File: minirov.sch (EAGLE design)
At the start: 69 parts, among them Q1 DMN6140L-13DICT-ND, Q2 DMN6140L-13DICT-ND, U1 DRV8848PWP, U2 DRV8848PWP, Y1 ECS-80-S-4X

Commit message: first iteration of schematic and board placements
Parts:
- removed C1, C10, C2, C3, C4, C5, C6, C7, C8, C9: 4.7uF, SparkFun-Capacitors:4.7UF0603
- removed C11: 0.1uF, SparkFun-Capacitors:0.1UF-0603-25V-(+80/-20%)
- removed R1, R10, R11, R2, R3: 1k, SparkFun-Resistors:1KOHM-0603-1/10W-1%
- removed RESET: SWITCH, DiscreteComponents:SWITCH
- removed SV1: (no value), con-lsta:FE05-1
- removed Y1: ECS-80-S-4X, ECS-80-S-4X:ECS-80-S-4X
- added C19: 100nF, SparkFun-Capacitors:10NF-0603-50V-10%
- added J21: (no value), SparkFun-Connectors:CONN_01
- added U$8: TLE493DW2B6, TLE493DW2B6:TLE493DW2B6
- added U$9: RPI-ZERO, RPI-Zero:RPI-ZERO
- U$2: value TCAN337D -> 74CBTLV3257PW; device PI_Shield_Library:TCAN337D -> 74CBTLV3257PW:74CBTLV3257PW
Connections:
- removed net N$3: C11.2, R10.1, R11.2
- removed net NRST: C7.1, R2.1, RESET.P$2, SV1.2, U$1.NRST
- removed net PWM3: U2.AIN1
- removed net PWM4: U2.AIN2
- new net MTR1_PWM: U$2.1A, U$9.GPIO13
- new net MTR2_PWM: U$2.2A, U$9.GPIO18
- new net MTR_AB_SEL: U$2.S, U$9.GEN4/GPIO23
- new net MTR_NOE: U$2.NOE, U$9.GPIO22/GEN3
- net +3V3: now also C19.2, J21.1, U$2.3V3, U$8.3V3; no longer C1.1, C10.1, C2.1, C3.1, C4.1, C5.1, C6.1, R2.2, SV1.5, U$1.VDD, U$1.VDDA, U$1.VDDIO2, U$2.VCC
- net +5V: now also U$9.5V0@1, U$9.5V0@2
- net CAN_H: no longer R10.2, U$2.CANH
- net CAN_L: no longer R11.1, U$2.CANL
- net CAN_STM_RX: no longer U$2.TXD
- net CAN_STM_TX: no longer U$2.RXD
- net GND: now also C19.1, U$8.GND1, U$8.GND2, U$8.GND3, U$9.GND@1, U$9.GND@2, U$9.GND@3, U$9.GND@4, U$9.GND@5, U$9.GND@6, U$9.GND@7, U$9.GND@8; no longer C1.2, C10.2, C11.1, C2.2, C3.2, C4.2, C5.2, C6.2, C7.2, C8.2, C9.2, RESET.P$1, SV1.1
- net LED1_PWM: now also U$9.GPIO17/GEN0; no longer U$1.PA6
- net LED2_PWM: now also U$9.GPIO27/GEN2; no longer U$1.PA7
- net MISO: now also U$9.GPIO9/MISO; no longer U$1.PB4
- net MOSI: now also U$9.GPIO10/MOSI; no longer U$1.PB5
- net MTR_1A_PWM: now also U$2.1B1; no longer U$1.PA0
- net MTR_1B_PWM: now also U$2.1B2; no longer U$1.PA1
- net MTR_2A_PWM: now also U$2.2B1, U2.AIN1; no longer U$1.PA2
- net MTR_2B_PWM: now also U$2.2B2, U2.AIN2; no longer U$1.PA3
- net N$1: now also U$9.TXD0/GPIO14; no longer C9.1, R1.1, Y1.2
- net N$2: now also U$9.RXD0/GPIO15; no longer C8.1, R3.1, Y1.1
- net OSC_IN: no longer R3.2
- net OSC_OUT: no longer R1.2
- net SCK: now also U$9.GPIO11/SCLK; no longer U$1.PB3
- net SCL: now also U$8.SCL, U$9.GPIO3/SCL1; no longer U$1.PB6
- net SDA: now also U$8.SDA, U$9.GPIO2/SDA1; no longer U$1.PB7
- net SWCLK: no longer SV1.3
- net SWDIO: no longer SV1.4
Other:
- note added: "Magnetometer"
- note removed: "CAN TERMINATION"
- note removed: "CAN TRANSCEIVER"
- note removed: "Pin 1 (VDD)"
- note removed: "Pin 17 (VDDIO2)"
- note removed: "Pin 5 (VDDA)"

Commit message: first round of routing. need to gnd stitch
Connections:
- removed net 12V: U$4.VIN
- net +12V: now also U$4.VIN
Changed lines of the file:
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@@
 <pinref part="SUPPLY5" gate="G$1" pin="12V"/>
+</segment>
+<segment>
+<pinref part="U$4" gate="G$1" pin="VIN"/>
+<wire x1="160.02" y1="279.4" x2="152.4" y2="279.4" width="0.1524" layer="91"/>
+<wire x1="152.4" y1="279.4" x2="152.4" y2="281.94" width="0.1524" layer="91"/>
+<pinref part="SUPPLY2" gate="G$1" pin="12V"/>
+<label x="152.4" y="276.86" size="1.778" layer="95"/>
 </segment>
 </net>
@@
 </segment>
 </net>
-<net name="12V" class="0">
-<segment>
-<pinref part="U$4" gate="G$1" pin="VIN"/>
-<wire x1="160.02" y1="279.4" x2="152.4" y2="279.4" width="0.1524" layer="91"/>
-<wire x1="152.4" y1="279.4" x2="152.4" y2="281.94" width="0.1524" layer="91"/>
-<pinref part="SUPPLY2" gate="G$1" pin="12V"/>
-</segment>
-</net>

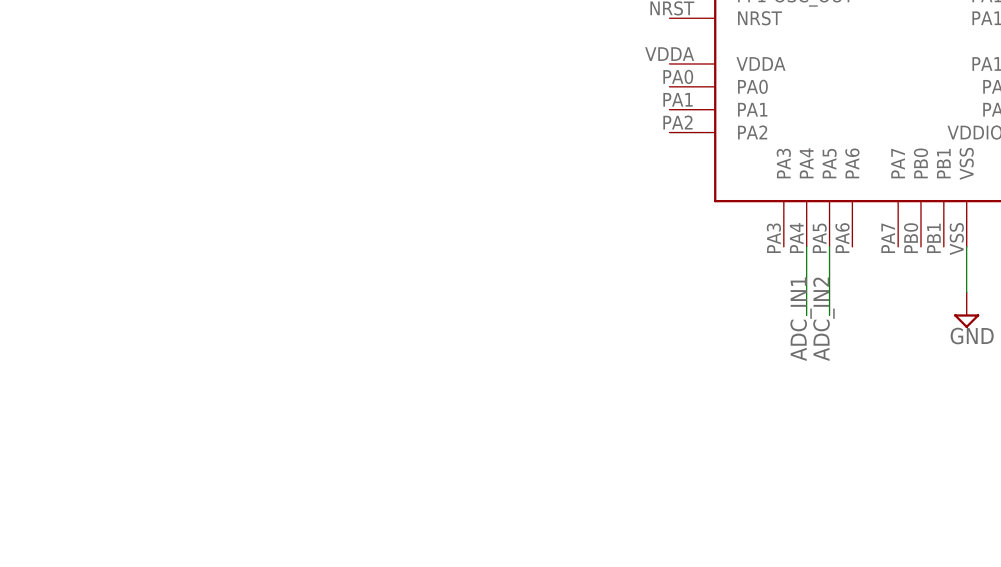
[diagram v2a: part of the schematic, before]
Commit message: added ADC
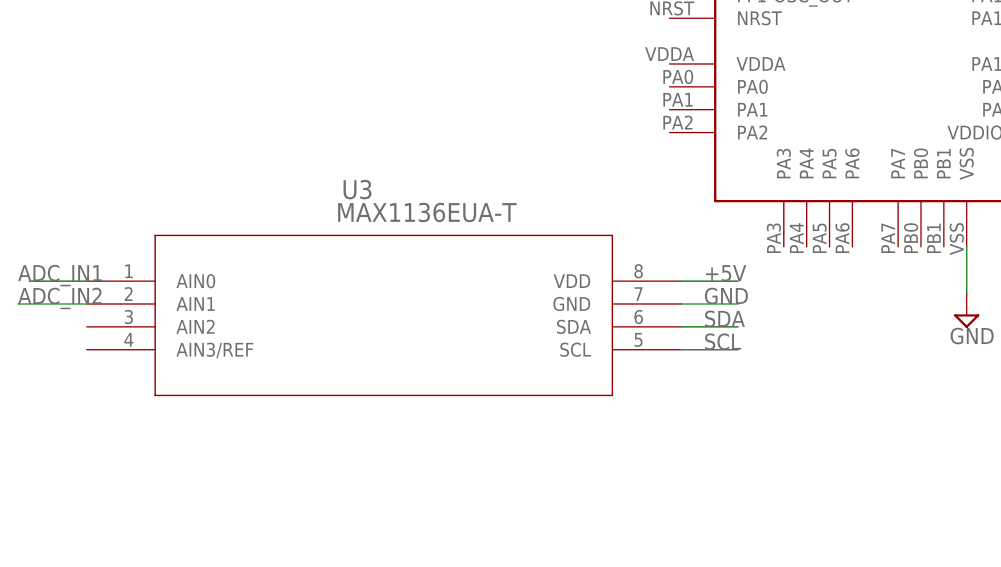
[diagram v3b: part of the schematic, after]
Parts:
- added U3: MAX1136EUA-T, MAX1136EUA-T:MAX1136EUA-T
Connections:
- net +5V: now also U3.VDD
- net ADC_IN1: now also U3.AIN0; no longer U$1.PA4
- net ADC_IN2: now also U3.AIN1; no longer U$1.PA5
- net GND: now also U3.GND
- net SCL: now also U3.SCL
- net SDA: now also U3.SDA
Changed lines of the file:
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@@
 <part name="GND3" library="supply1" library_urn="urn:adsk.eagle:library:371" deviceset="GND" device=""/>
 <part name="J21" library="SparkFun-Connectors" library_urn="urn:adsk.eagle:library:513" deviceset="CONN_01" device="" package3d_urn="urn:adsk.eagle:package:38028/1"/>
+<part name="U3" library="MAX1136EUA-T" deviceset="MAX1136EUA-T" device=""/>
 </parts>
 <sheets>
@@
 </instance>
 <instance part="J21" gate="G$1" x="81.28" y="246.38"/>
+<instance part="U3" gate="A" x="13.97" y="97.79" smashed="yes">
+<attribute name="NAME" x="42.3006" y="106.91988125" size="2.08538125" layer="95" ratio="6" rot="SR0"/>
+<attribute name="VALUE" x="41.6681" y="104.377509375" size="2.08561875" layer="96" ratio="6" rot="SR0"/>
+</instance>
 </instances>
 <busses>
@@
 <pinref part="GND3" gate="1" pin="GND"/>
 </segment>
+<segment>
+<pinref part="U3" gate="A" pin="GND"/>
+<wire x1="80.01" y1="95.25" x2="86.36" y2="95.25" width="0.1524" layer="91"/>
+<label x="82.55" y="95.25" size="1.778" layer="95"/>
+</segment>
 </net>
 <net name="SWDIO" class="0">
@@
 <net name="ADC_IN1" class="0">
 <segment>
-<pinref part="U$1" gate="G$1" pin="PA4"/>
-<wire x1="93.98" y1="101.6" x2="93.98" y2="93.98" width="0.1524" layer="91"/>
-<label x="93.98" y="88.9" size="1.778" layer="95" rot="R90"/>
-</segment>
-<segment>
 <pinref part="J13" gate="G$1" pin="1"/>
 <wire x1="88.9" y1="215.9" x2="96.52" y2="215.9" width="0.1524" layer="91"/>
 <label x="93.98" y="215.9" size="1.778" layer="95"/>
 </segment>
+<segment>
+<pinref part="U3" gate="A" pin="AIN0"/>
+<wire x1="7.62" y1="97.79" x2="13.97" y2="97.79" width="0.1524" layer="91"/>
+<label x="6.35" y="97.79" size="1.778" layer="95"/>
+</segment>
 </net>
 <net name="ADC_IN2" class="0">
-<segment>
-<pinref part="U$1" gate="G$1" pin="PA5"/>
-<wire x1="96.52" y1="101.6" x2="96.52" y2="93.98" width="0.1524" layer="91"/>
-<label x="96.52" y="88.9" size="1.778" layer="95" rot="R90"/>
-</segment>
 <segment>
 <pinref part="J14" gate="G$1" pin="1"/>
@@
 <label x="93.98" y="205.74" size="1.778" layer="95"/>
 </segment>
+<segment>
+<pinref part="U3" gate="A" pin="AIN1"/>
+<wire x1="13.97" y1="95.25" x2="6.35" y2="95.25" width="0.1524" layer="91"/>
+<label x="6.35" y="95.25" size="1.778" layer="95"/>
+</segment>
 </net>
 <net name="SDA" class="0">
@@
 <label x="149.86" y="104.14" size="1.778" layer="95"/>
 </segment>
+<segment>
+<pinref part="U3" gate="A" pin="SDA"/>
+<wire x1="80.01" y1="92.71" x2="86.36" y2="92.71" width="0.1524" layer="91"/>
+<label x="82.55" y="92.71" size="1.778" layer="95"/>
+</segment>
 </net>
 <net name="SCL" class="0">
@@
 <wire x1="157.48" y1="101.6" x2="152.4" y2="101.6" width="0.1524" layer="91"/>
 <label x="149.86" y="101.6" size="1.778" layer="95"/>
+</segment>
+<segment>
+<pinref part="U3" gate="A" pin="SCL"/>
+<wire x1="80.01" y1="90.17" x2="86.36" y2="90.17" width="0.1524" layer="91"/>
+<label x="82.55" y="90.17" size="1.778" layer="95"/>
 </segment>
 </net>
@@
 <label x="215.9" y="106.68" size="1.778" layer="95"/>
 </segment>
-</net>
+<segment>
+<pinref part="U3" gate="A" pin="VDD"/>
+<wire x1="80.01" y1="97.79" x2="86.36" y2="97.79" width="0.1524" layer="91"/>
+<label x="82.55" y="97.79" size="1.778" layer="95"/>
+</segment>
+</net>

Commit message: schematic changes and board changes to reflect it
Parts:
- removed C18: 10uF, SparkFun-Capacitors:10UF-0603-6.3V-20%
- removed D1: (no value), SparkFun-LED:LED0603
- removed J20, J6: (no value), SparkFun-Connectors:CONN_02
- removed J5: (no value), SparkFun-Connectors:CONN_04
- removed R12, R9: 0, SparkFun-Resistors:RESISTOR0603
- removed R6: (no value), SparkFun-Resistors:RESISTOR0603
- removed R7, R8: 10k, SparkFun-Resistors:RESISTOR0603
- removed U$1: STM32F042K6T6, PI_Shield_Library:STM32F042K6T6
- removed U$5: UN2112, minirov:UN2112
- removed U$6: UN2212, minirov:UN2212
- removed U$7: BAS16, minirov:BAS16
- removed U3: MAX1136EUA-T, MAX1136EUA-T:MAX1136EUA-T
- added C1: 100nF, SparkFun-Capacitors:10NF-0603-50V-10%
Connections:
- removed net CAN_H: J5.3
- removed net CAN_L: J5.2
- removed net CAN_STM_RX: U$1.PA11
- removed net CAN_STM_TX: U$1.PA12
- removed net HBEAT_LED: R6.1, U$1.PA15
- removed net N$1: U$9.TXD0/GPIO14
- removed net N$2: U$9.RXD0/GPIO15
- removed net N$4: D1.A, R6.2
- removed net N$5: C18.1, R8.1, U$7.1
- removed net OSC_IN: U$1.PF0-OSC_IN
- removed net OSC_OUT: U$1.PF1-OSC_OUT
- removed net RS-IN: J20.2, U$6.B, U$7.3
- removed net RS-OUT: J20.1, R8.2, U$5.C
- removed net RX: R12.1, U$5.B
- removed net SWCLK: U$1.PA14
- removed net SWDIO: U$1.PA13
- removed net TX: R7.1, R9.1, U$6.C
- removed net USART_RX: J6.1, R12.2, U$1.PA10
- removed net USART_TX: J6.2, R9.2, U$1.PA9
- net +12V: no longer J5.4
- net +3V3: now also C1.1; no longer R7.2, U$5.E
- net +5V: no longer U3.VDD
- net ADC_IN1: no longer U3.AIN0
- net ADC_IN2: no longer U3.AIN1
- net GND: now also C1.2; no longer C18.2, D1.C, J5.1, U$1.PB8-BOOT0, U$1.VSS, U$1.VSS1, U$6.E, U3.GND
- net SCL: no longer U3.SCL
- net SDA: no longer U3.SDA

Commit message: routing, deleting extraneous, and graphic
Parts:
- removed J13, J14: (no value), SparkFun-Connectors:CONN_01
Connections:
- removed net ADC_IN1: J13.1
- removed net ADC_IN2: J14.1
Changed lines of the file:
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@@
 <part name="J9" library="SparkFun-Connectors" library_urn="urn:adsk.eagle:library:513" deviceset="BANANA_CONN" device="" package3d_urn="urn:adsk.eagle:package:38018/1"/>
 <part name="J12" library="SparkFun-Connectors" library_urn="urn:adsk.eagle:library:513" deviceset="CONN_01" device="" package3d_urn="urn:adsk.eagle:package:38028/1"/>
-<part name="J13" library="SparkFun-Connectors" library_urn="urn:adsk.eagle:library:513" deviceset="CONN_01" device="" package3d_urn="urn:adsk.eagle:package:38028/1"/>
-<part name="J14" library="SparkFun-Connectors" library_urn="urn:adsk.eagle:library:513" deviceset="CONN_01" device="" package3d_urn="urn:adsk.eagle:package:38028/1"/>
 <part name="J15" library="SparkFun-Connectors" library_urn="urn:adsk.eagle:library:513" deviceset="CONN_02" device="" package3d_urn="urn:adsk.eagle:package:38039/1"/>
 <part name="Q1" library="minirov" deviceset="DMN6140L-13" device="" value="DMN6140L-13DICT-ND"/>
@@
 <instance part="J9" gate="G$1" x="86.36" y="269.24"/>
 <instance part="J12" gate="G$1" x="81.28" y="226.06"/>
-<instance part="J13" gate="G$1" x="81.28" y="215.9"/>
-<instance part="J14" gate="G$1" x="81.28" y="205.74"/>
 <instance part="J15" gate="G$1" x="119.38" y="231.14"/>
 <instance part="Q1" gate="G$1" x="309.88" y="317.5"/>
@@
 </segment>
 </net>
-<net name="ADC_IN1" class="0">
-<segment>
-<pinref part="J13" gate="G$1" pin="1"/>
-<wire x1="88.9" y1="215.9" x2="96.52" y2="215.9" width="0.1524" layer="91"/>
-<label x="93.98" y="215.9" size="1.778" layer="95"/>
-</segment>
-</net>
-<net name="ADC_IN2" class="0">
-<segment>
-<pinref part="J14" gate="G$1" pin="1"/>
-<wire x1="88.9" y1="205.74" x2="96.52" y2="205.74" width="0.1524" layer="91"/>
-<label x="93.98" y="205.74" size="1.778" layer="95"/>
-</segment>
-</net>

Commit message: Changes i forgot to push
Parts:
- removed H1, H2, H3, H4: STAND-OFF, SparkFun-Hardware:STAND-OFF
- added C10, C2, C3, C4, C5, C9: 0.1uF, SparkFun-Capacitors:0.1UF-0603-25V-(+80/-20%)
- added C11: 0.01uF, SparkFun-Capacitors:0.1UF-0603-25V-(+80/-20%)
- added C6: 10uF, SparkFun-Capacitors:0.1UF-0603-25V-(+80/-20%)
- added C7, C8: 18pF, SparkFun-Capacitors:0.1UF-0603-25V-(+80/-20%)
- added D1, D3: (no value), SparkFun-LED:LED-BLUE0603
- added D2, D4, D5: BLUE, SparkFun-LED:LED-BLUE0603
- added FB1: FERRITE_BEAD-0603, SparkFun-Coils:FERRITE_BEAD-0603
- added R1: 10k, SparkFun-Resistors:RESISTOR0603
- added R10, R11: 1k, SparkFun-Resistors:RESISTOR0603
- added R12, R13, R14: (no value), SparkFun-Resistors:RESISTOR0603
- added R2: 100k, SparkFun-Resistors:RESISTOR0603
- added R3: 2.2k 1%, SparkFun-Resistors:RESISTOR0603
- added R6, R7, R8, R9: 49.9 1%, SparkFun-Resistors:RESISTOR0603
- added U3: (no value), microbuilder:ENC28J60
- added U4: S811-1X1T-06-F, mini_rov_magjack:S811-1X1T-06-F
- added Y1: ABM8-25.000MHZ-B2-T, ABM8-25.000MHZ-B2-T:ABM8-25.000MHZ-B2-T
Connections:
- new net CS: R2.1, U$9.!CE0!/GPIO8, U3.CS
- new net INT: U$9.GEN/6GPIO25, U3.INT
- new net LEDA: R10.2, U3.LEDA
- new net LEDB: R11.2, U3.LEDB
- new net N$1: C7.2, U3.OSC1, Y1.1
- new net N$12: U3.WOL
- new net N$14: U3.CLKOUT
- new net N$2: C8.1, U3.OSC2, Y1.3
- new net N$25: R3.1, U3.RBIAS
- new net N$26: C6.1, U3.VCAP
- new net N$29: C10.2, FB1.2, R6.1, R7.1, U4.TCT
- new net N$3: D5.A, R12.1
- new net N$32: C11.1, R8.1, R9.1
- new net N$4: D1.A, R10.1
- new net N$5: D3.A, R11.1
- new net N$8: D2.A, R13.1
- new net N$9: D4.A, R14.1
- new net RST: R1.1, U3.RESET
- new net TPIN+: R8.2, U3.TPIN+, U4.RD+
- new net TPIN-: R9.2, U3.TPIN-, U4.RD-
- new net TPOUT+: R6.2, U3.TPOUT+, U4.TD+
- new net TPOUT-: R7.2, U3.TPOUT-, U4.TD-
- net +12V: now also R14.2
- net +3V3: now also C2.1, C3.1, C4.1, C5.1, C9.2, FB1.1, R1.2, R12.2, R2.2, U3.VDD, U3.VDD_OSC, U3.VDD_PLL, U3.VDD_RX, U3.VDD_TX
- net +5V: now also R13.2
- net GND: now also C10.1, C11.2, C2.2, C3.2, C4.2, C5.2, C6.2, C7.1, C8.2, C9.1, D1.C, D2.C, D3.C, D4.C, D5.C, R3.2, U3.VSS, U3.VSS_OSC, U3.VSS_PLL, U3.VSS_RX, U3.VSS_TX, Y1.GND
- net MISO: now also U3.SO
- net MOSI: now also U3.SI
- net SCK: now also U3.SCK
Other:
- note added: "311-49.9HRCT-ND - 49.9 1% resistor"
